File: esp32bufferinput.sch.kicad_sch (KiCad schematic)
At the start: 14 parts, among them U7 TL072, U8 TL072

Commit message: aded an stmsheet to see the symbol
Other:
- note added: "RIGHT AUDIO iNPUT"
- note added: "leftAUDIO IN"
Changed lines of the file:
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@@
+		)
+	)
+	(text "RIGHT AUDIO iNPUT\n"
+		(exclude_from_sim no)
+		(at 25.146 71.882 0)
+		(effects
+			(font
+				(size 1.27 1.27)
+				(thickness 0.254)
+				(bold yes)
+			)
+		)
+	)
+	(text "leftAUDIO IN\n"
+		(exclude_from_sim no)
+		(at 20.574 36.322 0)
+		(effects
+			(font
+				(size 1.27 1.27)
+				(thickness 0.254)
+				(bold yes)
+			)
 		)
 	)

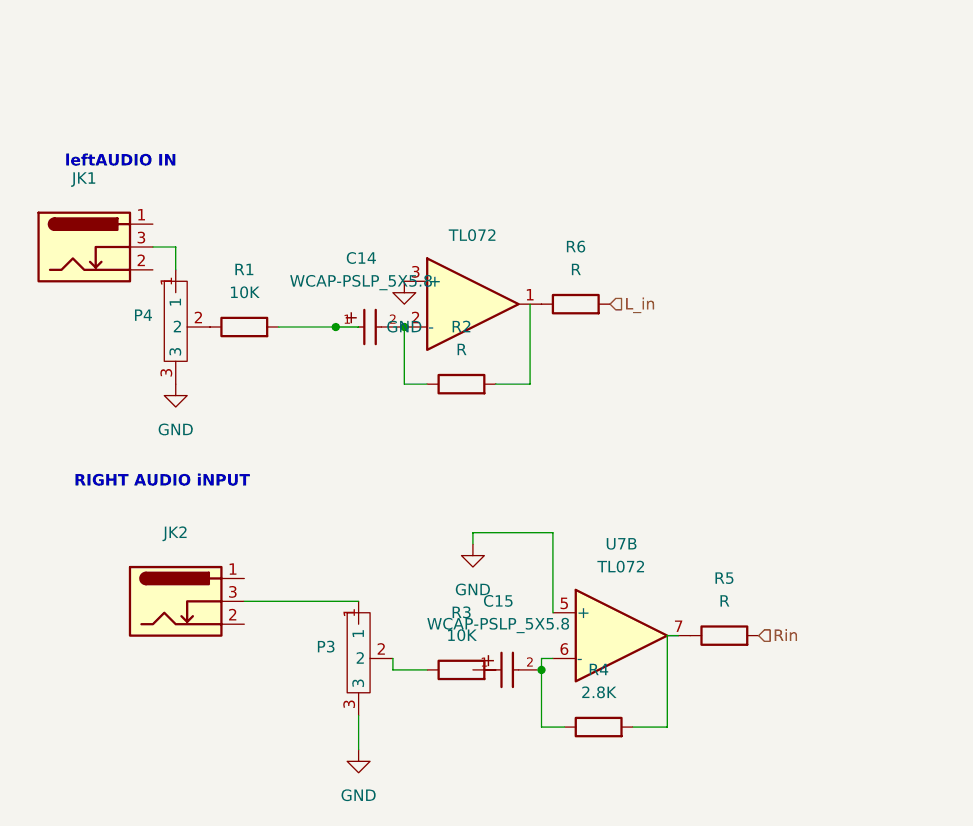
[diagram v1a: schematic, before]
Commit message: added pot model
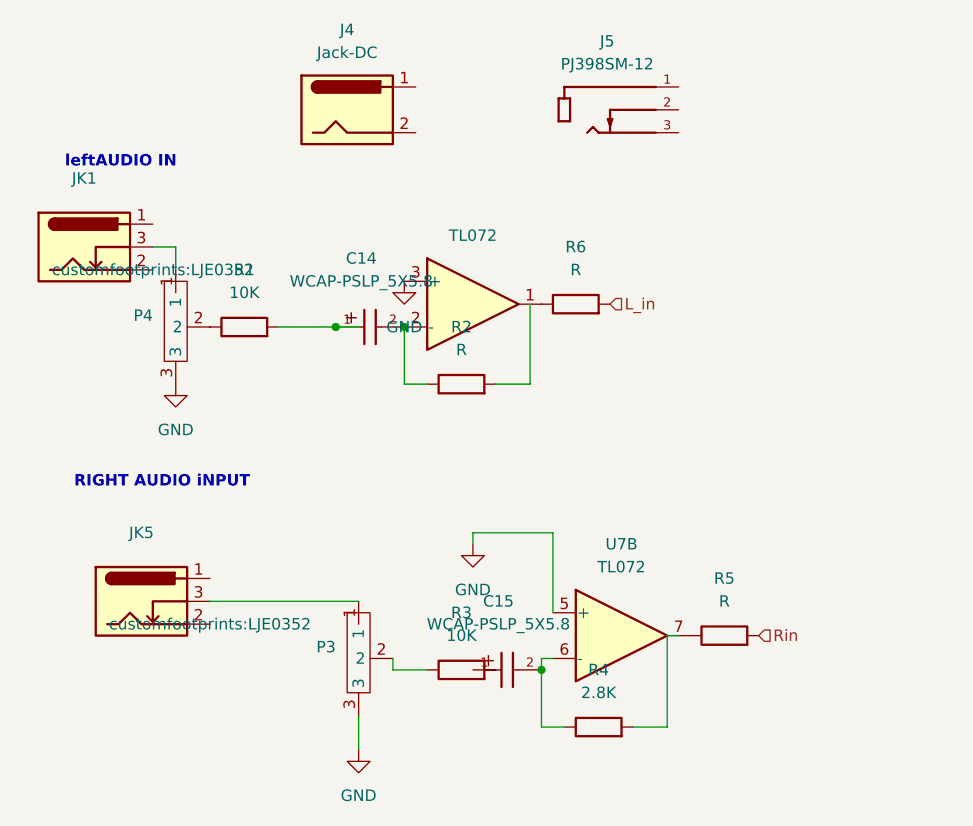
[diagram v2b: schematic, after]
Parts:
- removed JK2: ~, customfootprints:LJE0352, symbol esp32lib:LJE0352
- added J4: Jack-DC, symbol Connector:Jack-DC
- added J5: PJ398SM-12, customfootprints:THONK_PJ398SM-12, symbol esp32lib:PJ398SM-12
- added JK5: ~, customfootprints:LJE0352, symbol esp32lib:LJE0352
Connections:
- net at P3.1: now also JK5.3

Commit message: updated DacSheet
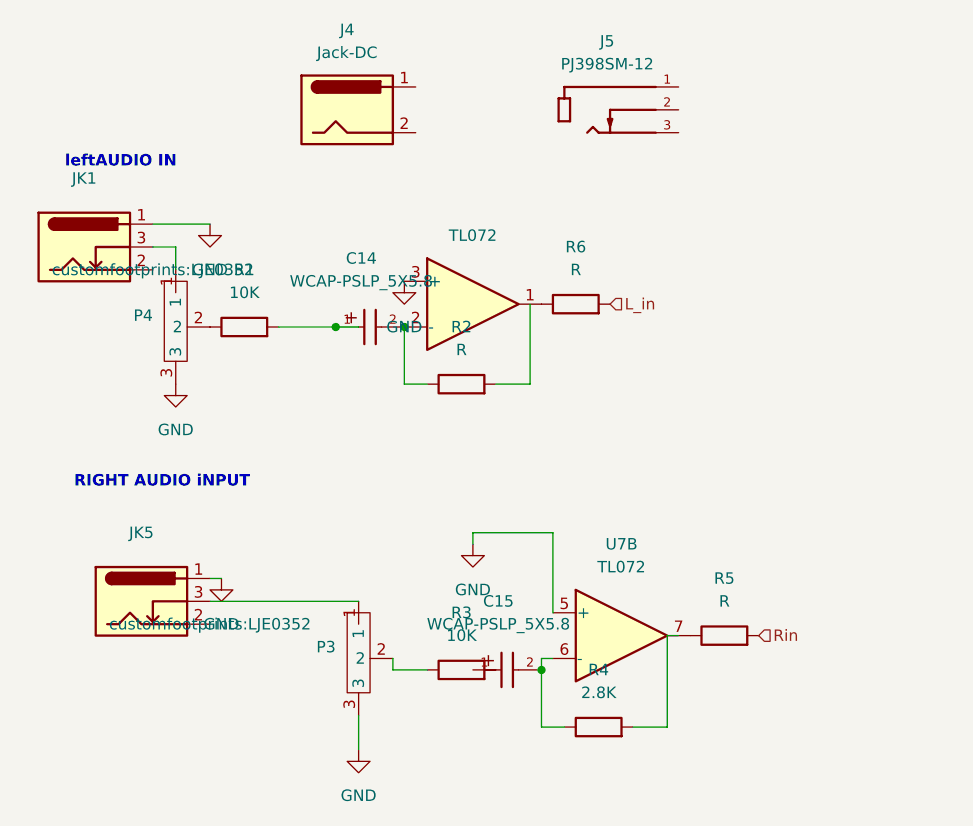
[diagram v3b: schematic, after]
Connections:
- net GND: now also JK1.1, JK5.1
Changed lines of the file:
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@@
+	(wire
+		(pts
+			(xy 30.48 82.55) (xy 31.75 82.55)
+		)
+		(stroke
+			(width 0)
+			(type default)
+		)
+	)
 	(wire
 		(pts
@@
 		(pts
 			(xy 68.58 86.36) (xy 68.58 77.47)
+		)
+		(stroke
+			(width 0)
+			(type default)
+		)
+	)
+	(wire
+		(pts
+			(xy 24.13 43.18) (xy 30.48 43.18)
 		)
 		(stroke
@@
 	)
 	(symbol
+		(lib_id "power:GND")
+		(at 31.75 82.55 0)
+		(unit 1)
+		(exclude_from_sim no)
+		(in_bom yes)
+		(on_board yes)
+		(dnp no)
+		(fields_autoplaced yes)
+		(property "Reference" "#PWR79"
+			(at 31.75 88.9 0)
+			(effects
+				(font
+					(size 1.27 1.27)
+				)
+				(hide yes)
+			)
+		)
+		(property "Value" "GND"
+			(at 31.75 87.63 0)
+			(effects
+				(font
+					(size 1.27 1.27)
+				)
+			)
+		)
+		(property "Footprint" ""
+			(at 31.75 82.55 0)
+			(effects
+				(font
+					(size 1.27 1.27)
+				)
+				(hide yes)
+			)
+		)
+		(property "Datasheet" ""
+			(at 31.75 82.55 0)
+			(effects
+				(font
+					(size 1.27 1.27)
+				)
+				(hide yes)
+			)
+		)
+		(property "Description" "Power symbol creates a global label with name \"GND\" , ground"
+			(at 31.75 82.55 0)
+			(effects
+				(font
+					(size 1.27 1.27)
+				)
+				(hide yes)
+			)
+		)
+		(pin "1"
+		)
+		(instances
+			(project ""
+				(path "/c4754426-a41b-4341-9d09-2e389619f3d6/32d637b3-b81c-4082-b7fa-739e0cc157fd/c3ee90a3-3bf6-46a1-8e78-8639215a2e13"
+					(reference "#PWR79")
+					(unit 1)
+				)
+			)
+		)
+	)
+	(symbol
 		(lib_id "Amplifier_Operational:TL072")
 		(at 76.2 88.9 0)
@@
 					(unit 1)
 				)
+			)
+		)
+	)
+	(symbol
+		(lib_id "power:GND")
+		(at 30.48 43.18 0)
+		(unit 1)
+		(exclude_from_sim no)
+		(in_bom yes)
+		(on_board yes)
+		(dnp no)
+		(fields_autoplaced yes)
+		(property "Reference" "#PWR80"
+			(at 30.48 49.53 0)
+			(effects
+				(font
+					(size 1.27 1.27)
+				)
+				(hide yes)
+			)
+		)
+		(property "Value" "GND"
+			(at 30.48 48.26 0)
+			(effects
+				(font
+					(size 1.27 1.27)
+				)
+			)
+		)
+		(property "Footprint" ""
+			(at 30.48 43.18 0)
+			(effects
+				(font
+					(size 1.27 1.27)
+				)
+				(hide yes)
+			)
+		)
+		(property "Datasheet" ""
+			(at 30.48 43.18 0)
+			(effects
+				(font
+					(size 1.27 1.27)
+				)
+				(hide yes)
+			)
+		)
+		(property "Description" "Power symbol creates a global label with name \"GND\" , ground"
+			(at 30.48 43.18 0)
+			(effects
+				(font
+					(size 1.27 1.27)
+				)
+				(hide yes)
+			)
+		)
+		(pin "1"
+		)
+		(instances
+			(project ""
+				(path "/c4754426-a41b-4341-9d09-2e389619f3d6/32d637b3-b81c-4082-b7fa-739e0cc157fd/c3ee90a3-3bf6-46a1-8e78-8639215a2e13"
+					(reference "#PWR80")
+					(unit 1)
+				)

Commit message: added codec buffers
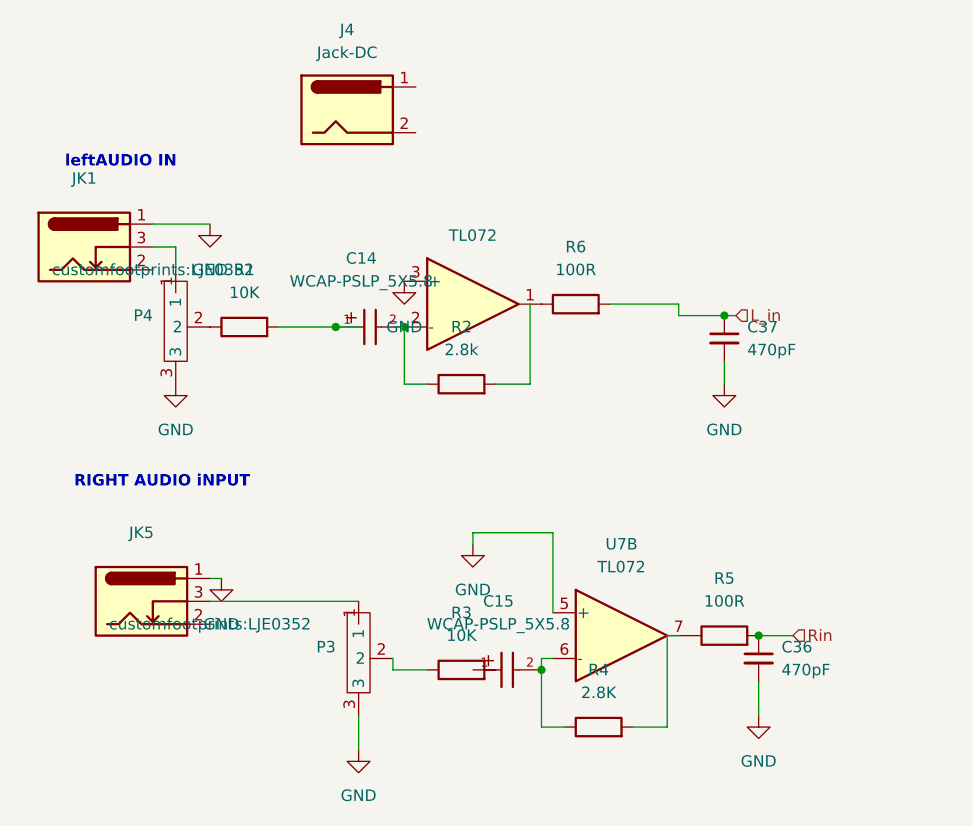
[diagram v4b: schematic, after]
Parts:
- removed J5: PJ398SM-12, customfootprints:THONK_PJ398SM-12, symbol esp32lib:PJ398SM-12
- added C36, C37: 470pF, symbol Device:C_Small
- R2: value R -> 2.8k
- R5, R6: value R -> 100R
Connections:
- net GND: now also C36.2, C37.2
- net L_in: now also C37.1
- net Rin: now also C36.1

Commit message: updated a few part values in the audio buffer input
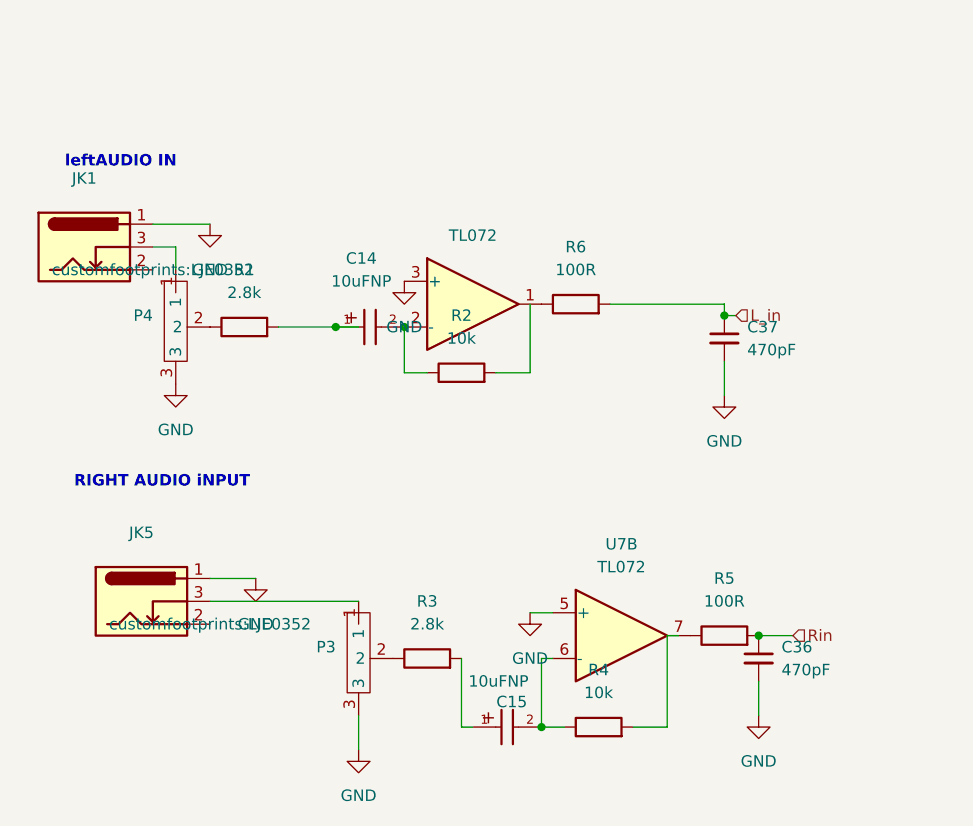
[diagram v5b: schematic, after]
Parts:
- removed J4: Jack-DC, symbol Connector:Jack-DC
- C14, C15: value WCAP-PSLP_5X5.8 -> 10uFNP
- R1: value 10K -> 2.8k; footprint (none) -> Resistor_SMD:R_0603_1608Metric
- R2: value 2.8k -> 10k
- R3: value 10K -> 2.8k
- R4: value 2.8K -> 10k
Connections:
- net at C15.1: now also R3.2
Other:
- moved on the sheet: C15, R2, R3

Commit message: updated common lib symbols and footprint models
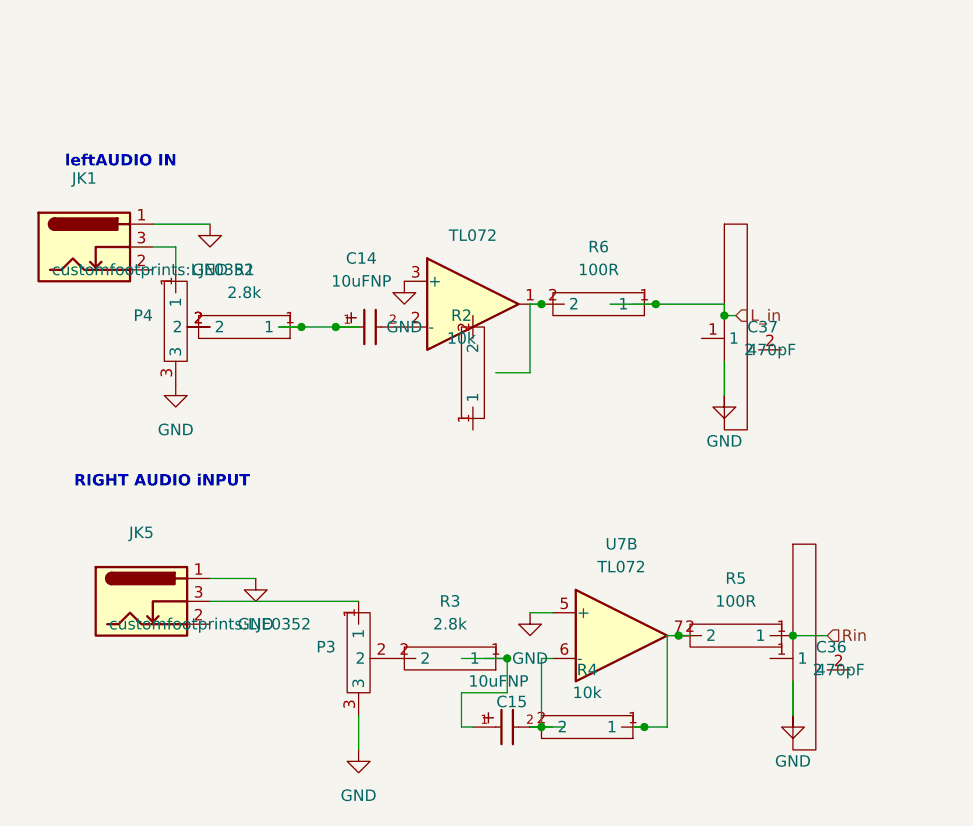
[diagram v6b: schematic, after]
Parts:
- C36, C37: footprint (none) -> commonfootprint:Ceramic0603; symbol Device:C_Small -> common:CerCap
- R1: footprint Resistor_SMD:R_0603_1608Metric -> commonfootprint:Modcan0603; symbol Device:R -> common:R
- R2, R3, R4, R5, R6: footprint (none) -> commonfootprint:Modcan0603; symbol Device:R -> common:R
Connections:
- net GND: no longer C36.2, C37.2
- net L_in: now also R6.1; no longer C37.1, R6.2
- net Rin: now also R5.1; no longer C36.1, R5.2
- net at U8.1: now also R6.2; no longer R6.1
- net at C15.2, U7.6 (-): now also R4.2; no longer R4.1
- net at U7.7: now also R4.1, R5.2; no longer R5.1
- net at P4.2: no longer R1.1
- net at C14.2, U8.2 (-): no longer R2.1
- net at C15.1: now also R3.1; no longer R3.2
- net at C14.1: now also R1.1; no longer R1.2
- net at P3.2: now also R3.2; no longer R3.1

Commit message: updated a few caps
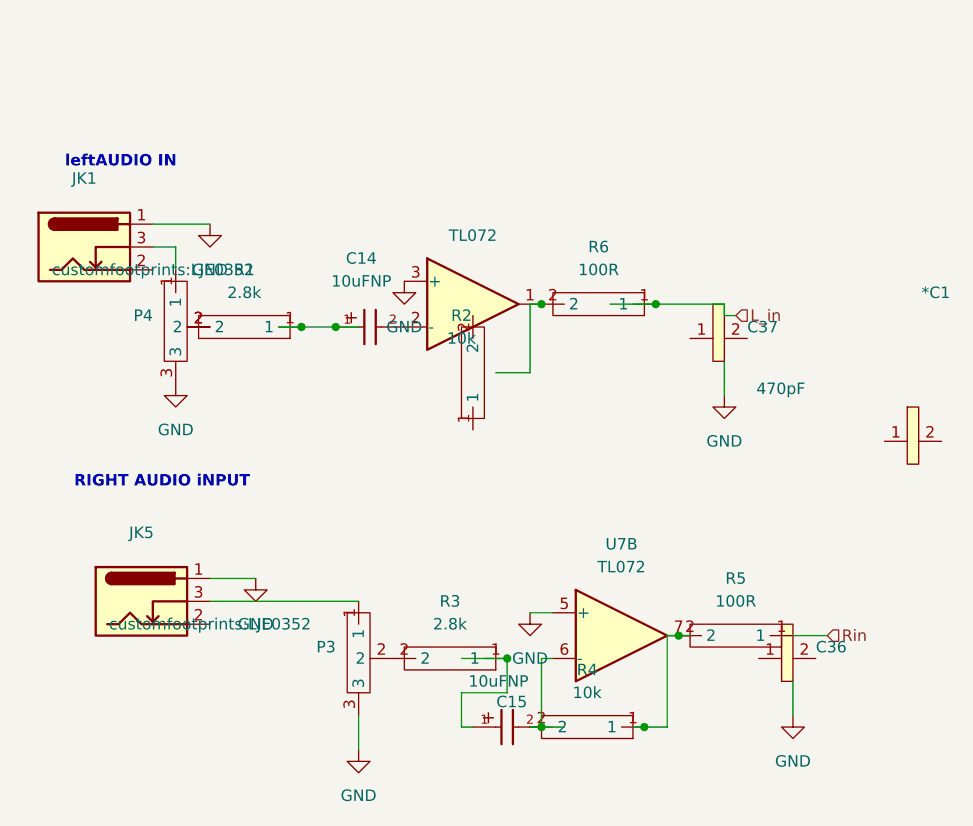
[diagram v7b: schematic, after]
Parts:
- added *C1: ~, commonfootprint:Ceramic0603, symbol common:CerCap
- C36: value 470pF -> ~
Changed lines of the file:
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@@
-	)
-	(junction
-		(at 87.63 53.34)
-		(diameter 0)
-		(color 0 0 0 0)
-	)
-	(junction
-		(at 95.25 88.9)
-		(diameter 0)
-		(color 0 0 0 0)
 	)
 	(junction
@@
 	)
 	(symbol
+		(lib_id "common:CerCap")
+		(at 109.22 67.31 0)
+		(unit 1)
+		(exclude_from_sim no)
+		(in_bom yes)
+		(on_board yes)
+		(dnp no)
+		(fields_autoplaced yes)
+		(property "Reference" "*C1"
+			(at 111.125 50.8 0)
+			(effects
+				(font
+					(size 1.27 1.27)
+				)
+			)
+		)
+		(property "Value" "~"
+			(at 111.125 53.34 0)
+			(effects
+				(font
+					(size 1.27 1.27)
+				)
+			)
+		)
+		(property "Footprint" "commonfootprint:Ceramic0603"
+			(at 109.22 67.31 0)
+			(effects
+				(font
+					(size 1.27 1.27)
+				)
+				(hide yes)
+			)
+		)
+		(property "Datasheet" ""
+			(at 109.22 67.31 0)
+			(effects
+				(font
+					(size 1.27 1.27)
+				)
+				(hide yes)
+			)
+		)
+		(property "Description" ""
+			(at 109.22 67.31 0)
+			(effects
+				(font
+					(size 1.27 1.27)
+				)
+				(hide yes)
+			)
+		)
+		(pin "1"
+		)
+		(pin "2"
+		)
+		(instances
+			(project ""
+				(path "/c4754426-a41b-4341-9d09-2e389619f3d6/32d637b3-b81c-4082-b7fa-739e0cc157fd/c3ee90a3-3bf6-46a1-8e78-8639215a2e13"
+					(reference "*C1")
+					(unit 1)
+				)
+			)
+		)
+	)
+	(symbol
 		(lib_id "common:R")
 		(at 57.15 92.71 180)
@@
 		)
 		(property "Value" "470pF"
-			(at 90.17 57.1562 0)
+			(at 91.186 61.468 0)
 			(effects
 				(font
@@
 		)
 		(property "Footprint" "commonfootprint:Ceramic0603"
-			(at 87.63 55.88 0)
+			(at 87.122 50.546 0)
 			(effects
 				(font
@@
 			)
 		)
-		(property "Description" "Unpolarized capacitor, small symbol"
+		(property "Description" ""
 			(at 87.63 55.88 0)
 			(effects
@@
 			)
 		)
-		(property "Value" "470pF"
+		(property "Value" "~"
 			(at 97.79 92.7162 0)
 			(effects
@@
 		)
 		(property "Footprint" "commonfootprint:Ceramic0603"
-			(at 95.25 91.44 0)
+			(at 97.028 87.376 0)
 			(effects
 				(font
@@
 			)
 		)
-		(property "Description" "Unpolarized capacitor, small symbol"
-			(at 95.25 91.44 0)
-			(effects
-				(font
+		(property "Description" ""
+			(at 94.996 85.344 0)
+			(effects
+				(font
